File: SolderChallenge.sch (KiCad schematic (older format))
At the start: 33 parts, among them Q1 MOS_N, Q2 MOS_N, Q3 MOS_N, Q4 MOS_N_x2, U1 555, U2 555, U3 555

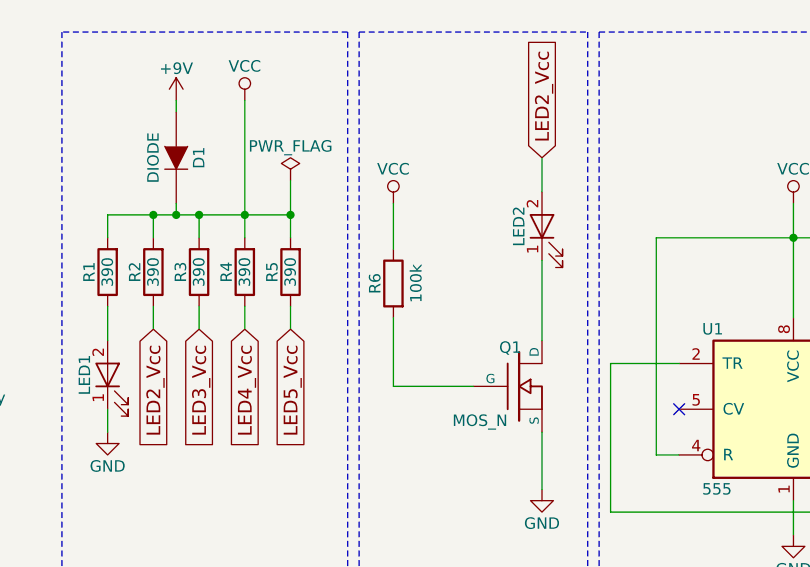
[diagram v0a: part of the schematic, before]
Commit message: Add manufacturers part number to schematic symbols
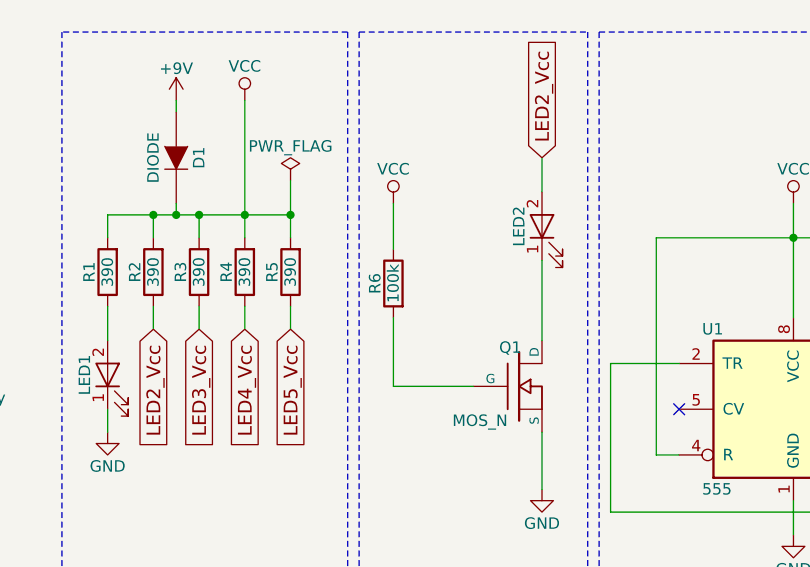
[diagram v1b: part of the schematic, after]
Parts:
- C1: manf_num (none) -> RDER71H225K2M1H03A
- C2: manf_num (none) -> CL31B225KOHNNNF
- C3: manf_num (none) -> C2012X7R1C225K125AB
- D1: manf_num (none) -> FR105G-K R0G
- LED1, LED2: manf_num (none) -> LTL-307E
- LED3: manf_num (none) -> LS T67K-K1L2-1
- LED4: manf_num (none) -> KPT-2012EC
- LED5: manf_num (none) -> SML-D12U1WT86
- Q1: manf_num (none) -> 2N7000-D26Z
- Q2, Q3: manf_num (none) -> NX7002AK\\,215
- Q4: manf_num (none) -> 2N7002PV\\,115
- R1, R2, R3, R4, R5: manf_num (none) -> MBB02070C3900FCT00
- R10, R11, R9: manf_num (none) -> CRG1206F100K
- R12, R13, R14: manf_num (none) -> MCR10EZPF1003
- R15, R16: manf_num (none) -> RK73H1JTTD1003F
- R6, R7, R8: manf_num (none) -> CFR16J100K
- U1: manf_num (none) -> NE555P
- U2: manf_num (none) -> NE555DR
- U3: manf_num (none) -> NE555PWR
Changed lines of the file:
@@
 F 2 "SolderChallenge:D_DO-41_SOD81_P7.62mm_Horizontal" H 2650 1100 60  0001 C CNN
 F 3 "" H 2650 1100 60  0000 C CNN
+F 4 "FR105G-K R0G" H 2650 1100 50  0001 C CNN "manf_num"
 	1    2650 1100
 	0    1    1    0
@@
 F 2 "SolderChallenge:LED_D5.0mm" H 2350 2050 50  0001 C CNN
 F 3 "" H 2350 2050 50  0001 C CNN
+F 4 "LTL-307E" H 2350 2050 50  0001 C CNN "manf_num"
 	1    2350 2050
 	0    -1   -1   0
@@
 F 2 "SolderChallenge:R_Axial_DIN0207_L6.3mm_D2.5mm_P9.00mm_Horizontal" V 2480 1600 50  0001 C CNN
 F 3 "" H 2550 1600 50  0001 C CNN
+F 4 "MBB02070C3900FCT00" V 2550 1600 50  0001 C CNN "manf_num"
 	1    2550 1600
 	-1   0    0    1
@@
 F 2 "SolderChallenge:R_Axial_DIN0207_L6.3mm_D2.5mm_P9.00mm_Horizontal" V 2680 1600 50  0001 C CNN
 F 3 "" H 2750 1600 50  0001 C CNN
+F 4 "MBB02070C3900FCT00" V 2750 1600 50  0001 C CNN "manf_num"
 	1    2750 1600
 	-1   0    0    1
@@
 F 2 "SolderChallenge:R_Axial_DIN0207_L6.3mm_D2.5mm_P9.00mm_Horizontal" V 2880 1600 50  0001 C CNN
 F 3 "" H 2950 1600 50  0001 C CNN
+F 4 "MBB02070C3900FCT00" V 2950 1600 50  0001 C CNN "manf_num"
 	1    2950 1600
 	-1   0    0    1
@@
 F 2 "SolderChallenge:LED_D3.0mm" H 4250 1400 50  0001 C CNN
 F 3 "" H 4250 1400 50  0001 C CNN
+F 4 "LTL-307E" H 4250 1400 50  0001 C CNN "manf_num"
 	1    4250 1400
 	0    -1   -1   0
@@
 P 3600 1650
 F 0 "R6" V 3680 1650 50  0000 C CNN
-F 1 "100k" V 3500 1650 50  0000 C CNN
+F 1 "100k" V 3600 1650 50  0000 C CNN
 F 2 "SolderChallenge:R_Axial_DIN0204_L3.6mm_D1.6mm_P5.08mm_Horizontal" V 3530 1650 50  0001 C CNN
 F 3 "" H 3600 1650 50  0001 C CNN
+F 4 "CFR16J100K" V 3600 1650 50  0001 C CNN "manf_num"
 	1    3600 1650
 	-1   0    0    -1
@@
 F 2 "SolderChallenge:DIP-8_W7.62mm" H 5350 2200 50  0001 C CNN
 F 3 "" H 5350 2200 50  0001 C CNN
+F 4 "NE555P" H 5350 2200 50  0001 C CNN "manf_num"
 	1    5350 2200
 	1    0    0    -1
@@
 F 2 "SolderChallenge:R_Axial_DIN0204_L3.6mm_D1.6mm_P5.08mm_Horizontal" V 6030 1750 50  0001 C CNN
 F 3 "" H 6100 1750 50  0001 C CNN
+F 4 "CFR16J100K" V 6100 1750 50  0001 C CNN "manf_num"
 	1    6100 1750
 	1    0    0    -1
@@
 F 2 "SolderChallenge:R_Axial_DIN0204_L3.6mm_D1.6mm_P5.08mm_Horizontal" V 6030 2450 50  0001 C CNN
 F 3 "" H 6100 2450 50  0001 C CNN
+F 4 "CFR16J100K" V 6100 2450 50  0001 C CNN "manf_num"
 	1    6100 2450
 	1    0    0    -1
@@
 F 2 "SolderChallenge:C_Disc_D5.1mm_W3.2mm_P5.00mm" H 6138 2750 50  0001 C CNN
 F 3 "" H 6100 2900 50  0001 C CNN
+F 4 "RDER71H225K2M1H03A" H 6100 2900 50  0001 C CNN "manf_num"
 	1    6100 2900
 	1    0    0    -1
@@
 F 2 "SolderChallenge:LED_PLCC-2" H 6900 1550 50  0001 C CNN
 F 3 "" H 6900 1550 50  0001 C CNN
+F 4 "LS T67K-K1L2-1" H 6900 1550 50  0001 C CNN "manf_num"
 	1    6900 1550
 	0    -1   -1   0
@@
 F 2 "SolderChallenge:SOT-23_GSD_Handsoldering" H 6800 2000 60  0001 C CNN
 F 3 "" H 6800 2000 60  0000 C CNN
+F 4 "NX7002AK\\,215" H 6800 2000 50  0001 C CNN "manf_num"
 	1    6800 2000
 	1    0    0    -1
@@
 F 2 "SolderChallenge:R_1206_HandSoldering" V 6380 1650 50  0001 C CNN
 F 3 "" H 6450 1650 50  0001 C CNN
+F 4 "CRG1206F100K" V 6450 1650 50  0001 C CNN "manf_num"
 	1    6450 1650
 	1    0    0    1
@@
 F 2 "SolderChallenge:SOIC-8_3.9x4.9mm_Pitch1.27mm" H 1700 5350 50  0001 C CNN
 F 3 "" H 1700 5350 50  0001 C CNN
+F 4 "NE555DR" H 1700 5350 50  0001 C CNN "manf_num"
 	1    1700 5350
 	1    0    0    -1
@@
 F 2 "SolderChallenge:R_1206_HandSoldering" V 2380 4900 50  0001 C CNN
 F 3 "" H 2450 4900 50  0001 C CNN
+F 4 "CRG1206F100K" V 2450 4900 50  0001 C CNN "manf_num"
 	1    2450 4900
 	1    0    0    -1
@@
 F 2 "SolderChallenge:R_1206_HandSoldering" V 2380 5600 50  0001 C CNN
 F 3 "" H 2450 5600 50  0001 C CNN
+F 4 "CRG1206F100K" V 2450 5600 50  0001 C CNN "manf_num"
 	1    2450 5600
 	1    0    0    -1
@@
 F 2 "SolderChallenge:C_1206_HandSoldering" H 2488 5900 50  0001 C CNN
 F 3 "" H 2450 6050 50  0001 C CNN
+F 4 "CL31B225KOHNNNF" H 2450 6050 50  0001 C CNN "manf_num"
 	1    2450 6050
 	1    0    0    -1
@@
 F 2 "SolderChallenge:R_Axial_DIN0207_L6.3mm_D2.5mm_P9.00mm_Horizontal" V 2280 1600 50  0001 C CNN
 F 3 "" H 2350 1600 50  0001 C CNN
+F 4 "MBB02070C3900FCT00" V 2350 1600 50  0001 C CNN "manf_num"
 	1    2350 1600
 	-1   0    0    1
@@
 F 2 "SolderChallenge:LED_0805_HandSoldering" H 3250 4700 50  0001 C CNN
 F 3 "" H 3250 4700 50  0001 C CNN
+F 4 "KPT-2012EC" H 3250 4700 50  0001 C CNN "manf_num"
 	1    3250 4700
 	0    -1   -1   0
@@
 F 2 "SolderChallenge:SOT-23_GSD_Nexperia_TO-236AB" H 3150 5150 60  0001 C CNN
 F 3 "" H 3150 5150 60  0000 C CNN
+F 4 "NX7002AK\\,215" H 3150 5150 50  0001 C CNN "manf_num"
 	1    3150 5150
 	1    0    0    -1
@@
 F 2 "SolderChallenge:R_0805_HandSoldering" V 2730 4800 50  0001 C CNN
 F 3 "" H 2800 4800 50  0001 C CNN
+F 4 "MCR10EZPF1003" V 2800 4800 50  0001 C CNN "manf_num"
 	1    2800 4800
 	1    0    0    1
@@
 F 2 "SolderChallenge:R_Axial_DIN0207_L6.3mm_D2.5mm_P9.00mm_Horizontal" V 3080 1600 50  0001 C CNN
 F 3 "" H 3150 1600 50  0001 C CNN
+F 4 "MBB02070C3900FCT00" V 3150 1600 50  0001 C CNN "manf_num"
 	1    3150 1600
 	-1   0    0    1
@@
 F 2 "SolderChallenge:TSSOP-8_4.4x3mm_Pitch0.65mm" H 4300 5350 50  0001 C CNN
 F 3 "" H 4300 5350 50  0001 C CNN
+F 4 "NE555PWR" H 4300 5350 50  0001 C CNN "manf_num"
 	1    4300 5350
 	1    0    0    -1
@@
 F 2 "SolderChallenge:R_0805_HandSoldering" V 4980 4900 50  0001 C CNN
 F 3 "" H 5050 4900 50  0001 C CNN
+F 4 "MCR10EZPF1003" V 5050 4900 50  0001 C CNN "manf_num"
 	1    5050 4900
 	1    0    0    -1
@@
 F 2 "SolderChallenge:R_0805_HandSoldering" V 4980 5600 50  0001 C CNN
 F 3 "" H 5050 5600 50  0001 C CNN
+F 4 "MCR10EZPF1003" V 5050 5600 50  0001 C CNN "manf_num"
 	1    5050 5600
 	1    0    0    -1
@@
 F 2 "SolderChallenge:C_0805_HandSoldering" H 5088 5900 50  0001 C CNN
 F 3 "" H 5050 6050 50  0001 C CNN
+F 4 "C2012X7R1C225K125AB" H 5050 6050 50  0001 C CNN "manf_num"
 	1    5050 6050
 	1    0    0    -1
@@
 F 2 "SolderChallenge:LED_0603_HandSoldering" H 6750 4950 50  0001 C CNN
 F 3 "" H 6750 4950 50  0001 C CNN
+F 4 "SML-D12U1WT86" H 6750 4950 50  0001 C CNN "manf_num"
 	1    6750 4950
 	0    -1   -1   0
@@
 F 2 "SolderChallenge:R_0603_HandSoldering" V 5330 5400 50  0001 C CNN
 F 3 "" H 5400 5400 50  0001 C CNN
+F 4 "RK73H1JTTD1003F" V 5400 5400 50  0001 C CNN "manf_num"
 	1    5400 5400
 	1    0    0    1
@@
 F 2 "SolderChallenge:R_0603_HandSoldering" V 5780 5250 50  0001 C CNN
 F 3 "" H 5850 5250 50  0001 C CNN
+F 4 "RK73H1JTTD1003F" V 5850 5250 50  0001 C CNN "manf_num"
 	1    5850 5250
 	1    0    0    1
@@
 F 2 "SolderChallenge:TO-92_Inline_Wide_SGD" H 4150 2100 60  0001 C CNN
 F 3 "" H 4150 2100 60  0000 C CNN
+F 4 "2N7000-D26Z" H 4150 2100 50  0001 C CNN "manf_num"
 	1    4150 2100
 	1    0    0    -1
@@
 F 2 "TO_SOT_Packages_SMD:SOT-363_SC-70-6" H 5950 5625 50  0001 L CIN
 F 3 "" H 5750 5700 50  0001 L CNN
+F 4 "2N7002PV\\,115" H 5750 5700 50  0001 C CNN "manf_num"
 	1    5750 5700
 	1    0    0    -1
